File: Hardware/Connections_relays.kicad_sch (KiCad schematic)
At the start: 58 parts, among them J1 USB4105-GF-A-120, J2 Conn_01x02, J3 1040310811, J4 Conn_01x02, J6 Conn_01x02, J7 Conn_01x02, Q2 NMOS, Q3 NMOS, Q4 NMOS, Q5 NMOS, U11 W25Q128JVS, U4 TPD2EUSB30DRTR

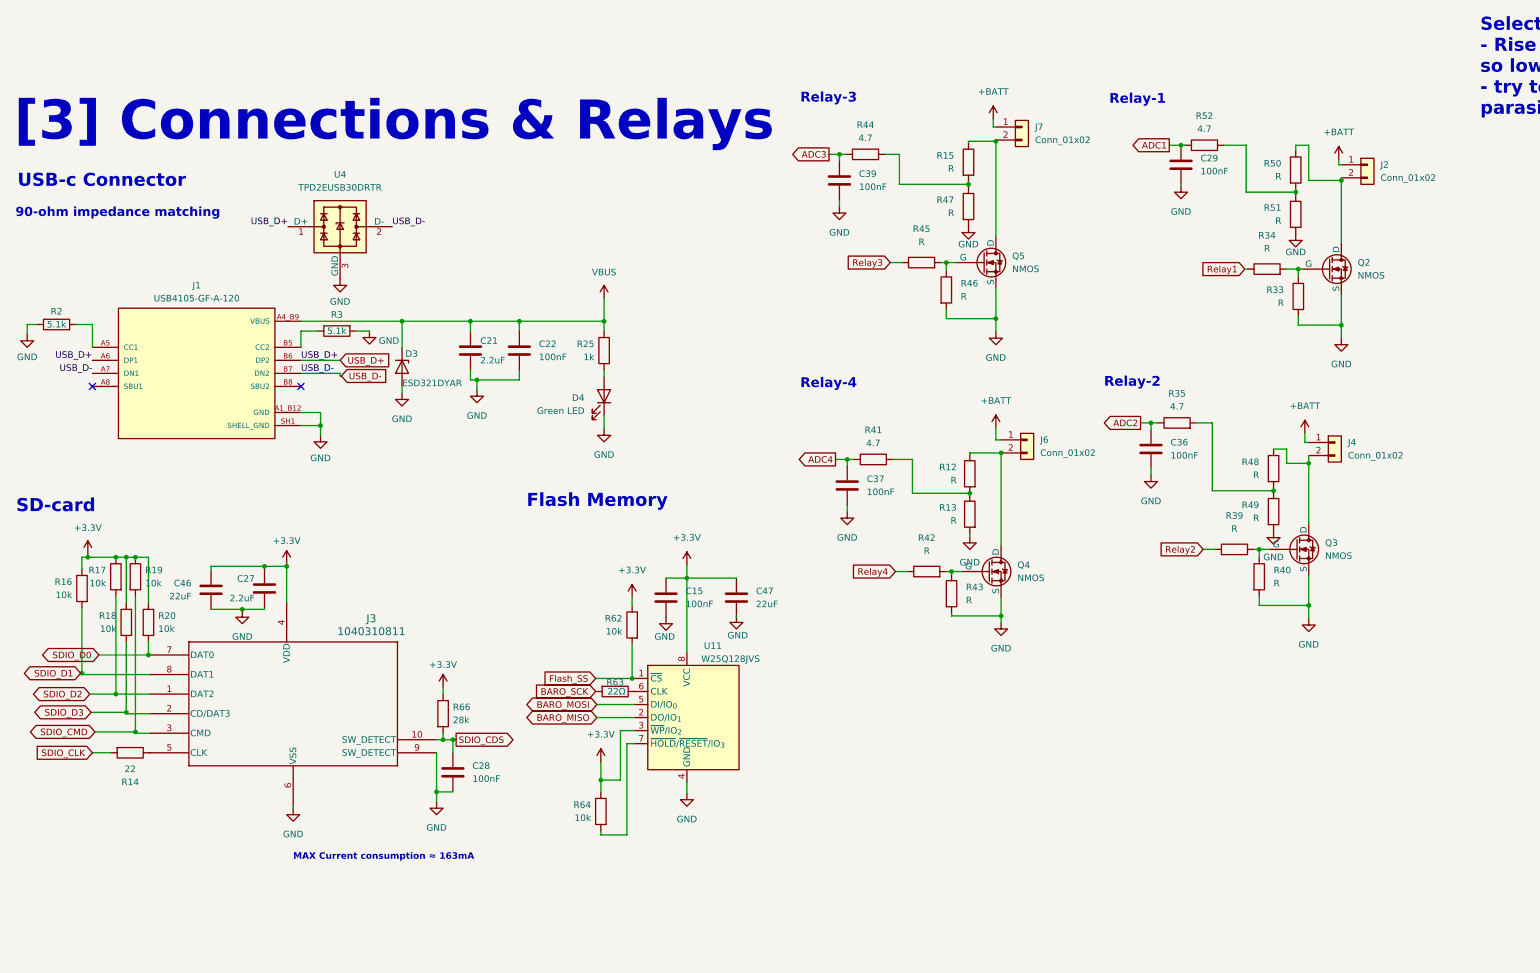
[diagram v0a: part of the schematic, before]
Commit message: Added New file for additional resources used, Changed LDO for lower noise, changed buck converter for higher switching speed, smaller inductance value, better transient current response
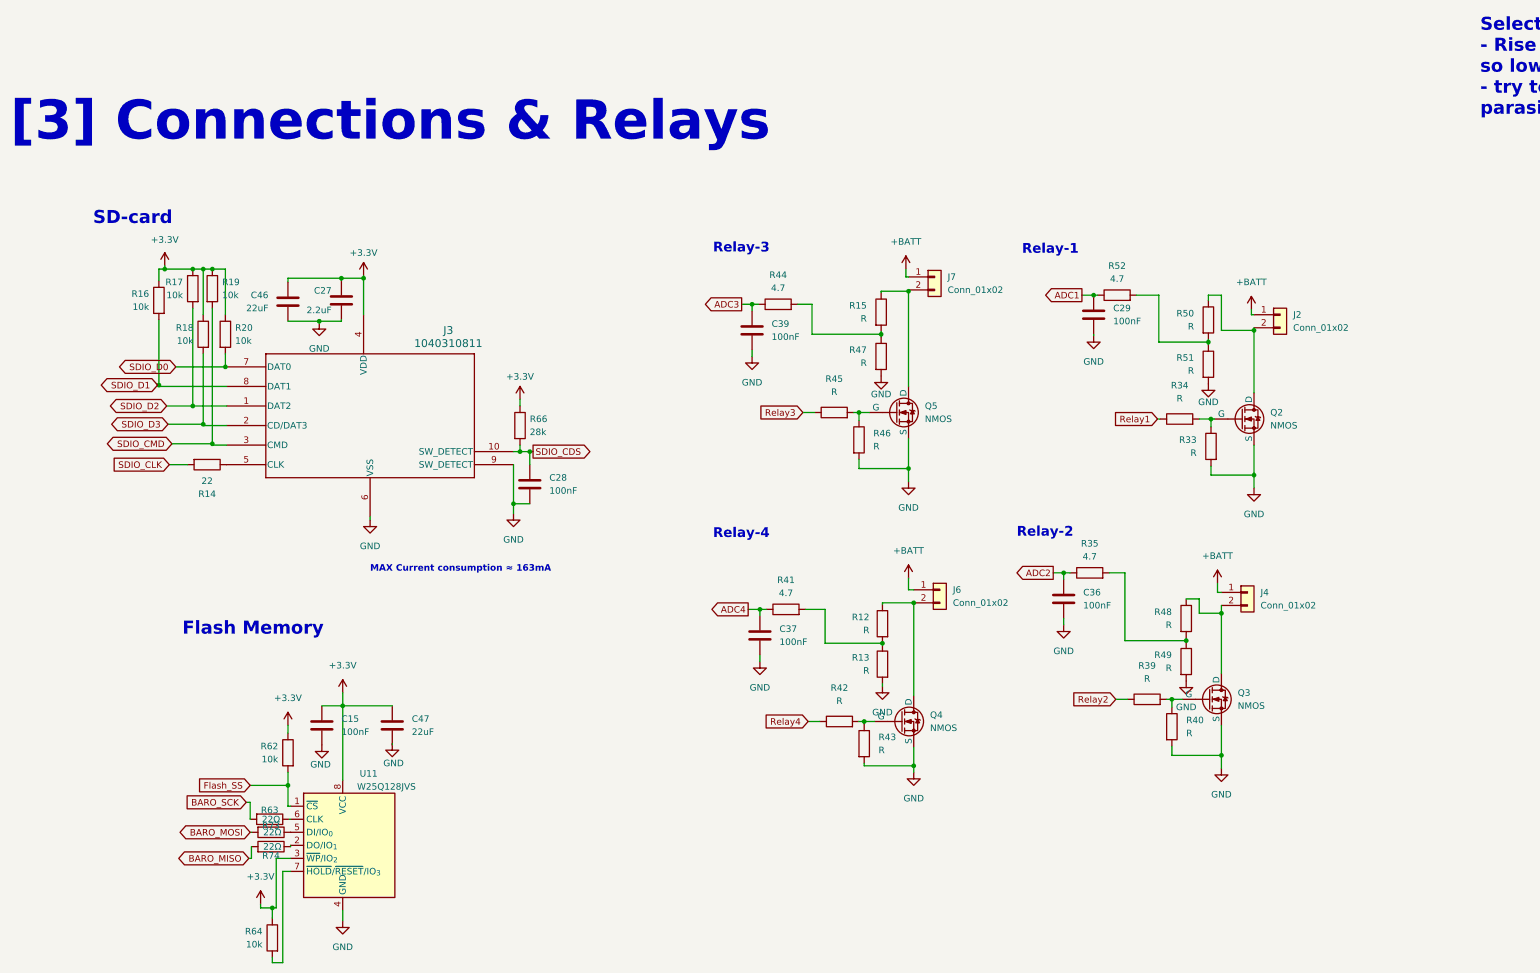
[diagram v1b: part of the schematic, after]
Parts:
- removed C21: 2.2uF, Capacitor_SMD:C_0402_1005Metric, symbol Device:C
- removed C22: 100nF, Capacitor_SMD:C_0402_1005Metric, symbol Device:C
- removed D3: ESD321DYAR, Diode_SMD:D_SOD-523, symbol Diode:ESD5Zxx
- removed D4: Green LED, LED_SMD:LED_0603_1608Metric, symbol Device:LED
- removed J1: USB4105-GF-A-120, USB4105-GF-A-120:GCT_USB4105-GF-A-120, symbol USB4105-GF-A-120:USB4105-GF-A-120
- removed R2, R3: 5.1k, Resistor_SMD:R_0402_1005Metric, symbol Device:R
- removed R25: 1k, Resistor_SMD:R_0402_1005Metric, symbol Device:R
- removed U4: TPD2EUSB30DRTR, Package_TO_SOT_SMD:Texas_DRT-3, symbol Power_Protection:TPD2EUSB30A
- added R73, R74: 22Ω, Resistor_SMD:R_0402_1005Metric, symbol Device:R
- U11: Distributer Link (none) -> https://www.ozdisan.com/en/p/embedded-memories-255/winbond-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; Part Number (none) -> W25Q32RVSSJQ
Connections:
- net BARO_MISO: now also R74.2; no longer U11.2 (DO/IO_{1})
- net BARO_MOSI: now also R73.2; no longer U11.5 (DI/IO_{0})
- new net: R73.1, U11.5 (DI/IO_{0})
- new net: R74.1, U11.2 (DO/IO_{1})
- no-connect marks 2 -> 0
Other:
- note removed: "90-ohm impedance matching"
- note removed: "USB-c Connector"
- moved on the sheet: C15, C27, C28, C29, C36, C37, C39, C46, C47, J2, J3, J4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

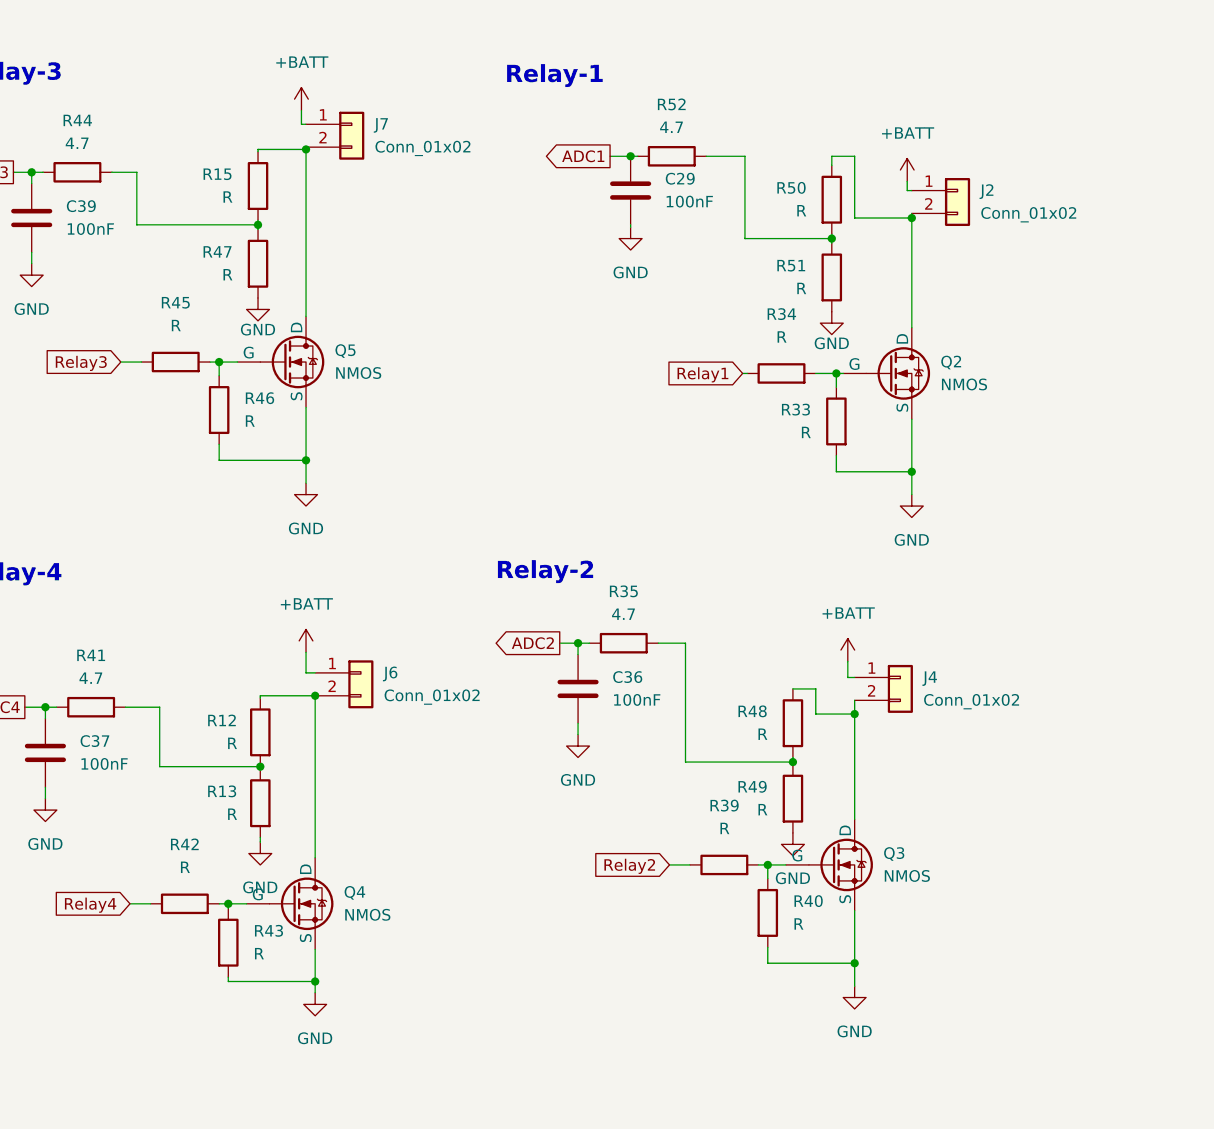
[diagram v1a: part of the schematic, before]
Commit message: Added Impedance matching calculations, finished buck converter calculations, finalized buzzer circuitry
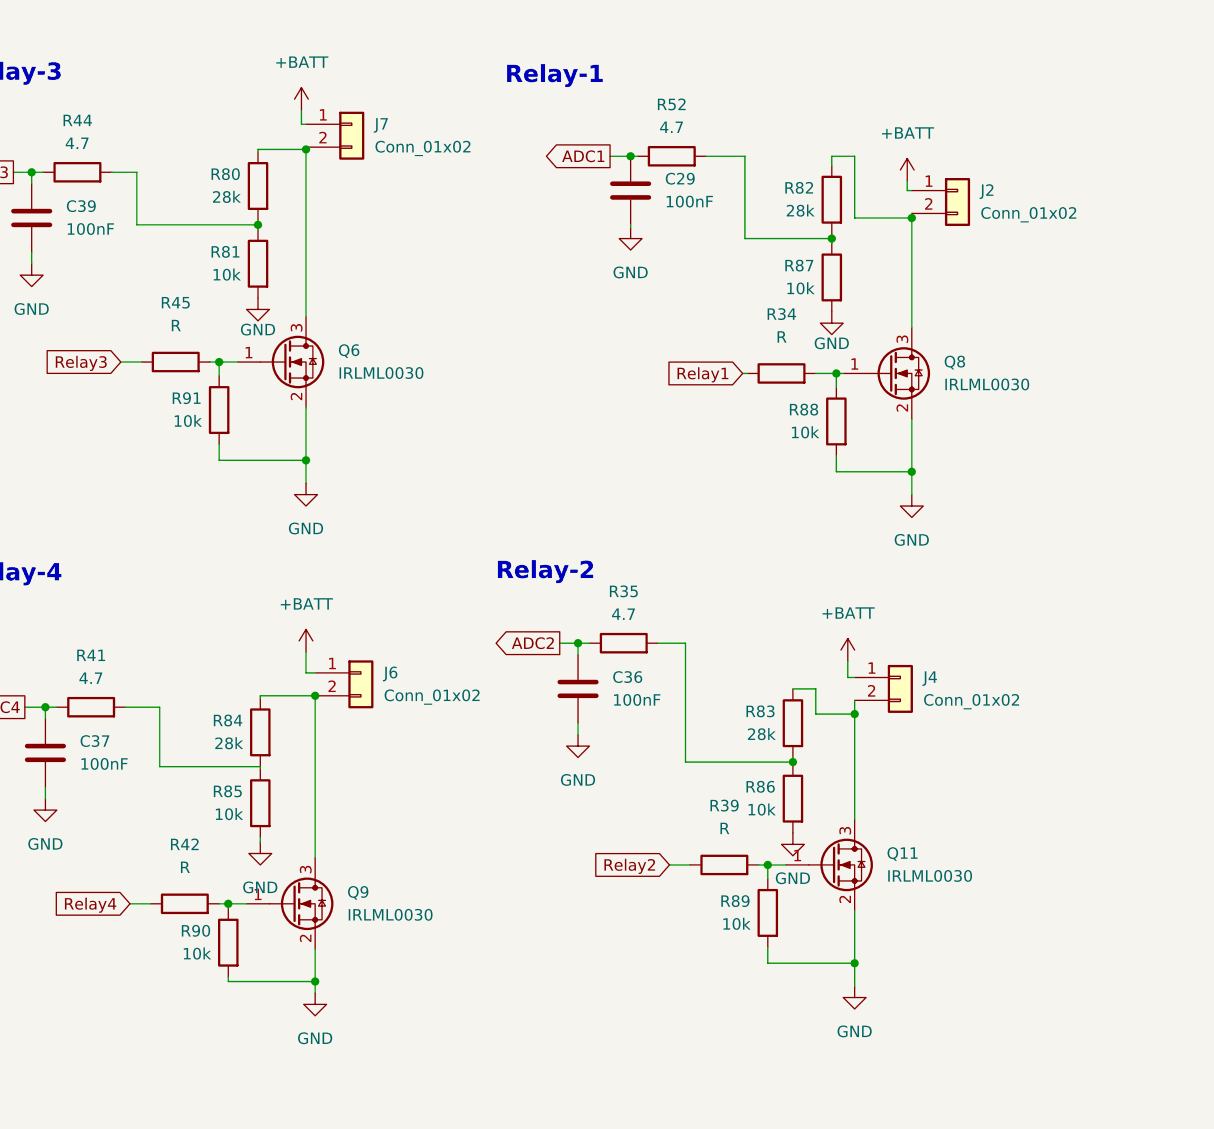
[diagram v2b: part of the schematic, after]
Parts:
- removed Q2, Q3, Q4, Q5: NMOS, symbol Simulation_SPICE:NMOS
- removed R12, R13, R15, R33, R40, R43, R46, R47, R48, R49, R50, R51: R, symbol Device:R
- added Q11, Q6, Q8, Q9: IRLML0030, Package_TO_SOT_SMD:SOT-23, symbol Transistor_FET:IRLML0030
- added R80, R82, R83, R84: 28k, Resistor_SMD:R_0402_1005Metric, symbol Device:R
- added R81, R85, R86, R87, R88, R89, R90, R91: 10k, Resistor_SMD:R_0402_1005Metric, symbol Device:R
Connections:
- net GND: now also Q11.2 (S), Q6.2 (S), Q8.2 (S), Q9.2 (S), R81.2, R85.2, R86.2, R87.2, R88.2, R89.2, R90.2, R91.2
- net at J7.2 (Pin_2): now also Q6.3 (D), R80.1
- net at R45.2: now also Q6.1 (G), R91.1
- net at R42.2: now also Q9.1 (G), R90.1
- net at R39.2: now also Q11.1 (G), R89.1
- net at R35.2: now also R83.2, R86.1
- net at R44.2: now also R80.2, R81.1
- net at R34.2: now also Q8.1 (G), R88.1
- net at R52.2: now also R82.2, R87.1
- net at J6.2 (Pin_2): now also Q9.3 (D), R84.1
- net at R41.2: now also R84.2, R85.1
- net at J4.2 (Pin_2): now also Q11.3 (D), R83.1
- net at J2.2 (Pin_2): now also Q8.3 (D), R82.1

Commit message: Changed footprints, generated BOM
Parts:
- removed R14: 22, Resistor_SMD:R_0402_1005Metric, symbol Device:R
- removed R16, R17, R18, R19, R20, R64: 10k, Resistor_SMD:R_0402_1005Metric, symbol Device:R
- removed R41, R44, R52: 4.7, Resistor_SMD:R_0402_1005Metric, symbol Device:R
- added R105: 22, Resistor_SMD:R_0603_1608Metric, symbol Device:R
- added R36, R37, R38: 4.7, Resistor_SMD:R_0603_1608Metric, symbol Device:R
- added R61, R77, R96, R97, R98, R99: 10k, Resistor_SMD:R_0603_1608Metric, symbol Device:R
- C15, C28, C29, C36, C37, C39: footprint Capacitor_SMD:C_0402_1005Metric -> Capacitor_SMD:C_0603_1608Metric; Distributer Link https://www.ozdisan.com/p/smt-smd-ve-mlcc-kapasitorler-184/murata-grt155r71e104ke01d-1074547 -> https://www.ozdisan.com/p/smt-smd-ve-mlcc-kapasitorler-184/samsung-cl10b104ko8wpnc-522227; Part Number GRT155R71E104KE01D -> CL10B104KO8WPNC
- C27: footprint Capacitor_SMD:C_0402_1005Metric -> Capacitor_SMD:C_0603_1608Metric; Distributer Link http://ozdisan.com/p/smt-smd-ve-mlcc-kapasitorler-184/murat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 -> https://www.ozdisan.com/p/smt-smd-ve-mlcc-kapasitorler-184/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; Part Number GRT155C81A225ME13D -> CL10B225KP8NNNC
- C47: value 22uF -> 2.2uF; footprint Capacitor_SMD:C_0805_2012Metric -> Capacitor_SMD:C_0603_1608Metric; Distributer Link https://www.ozdisan.com/p/smt-smd-ve-mlcc-kapasitorler-184/samsung-cl21a226koqnnne-399002 -> https://www.ozdisan.com/p/smt-smd-ve-mlcc-kapasitorler-184/samsung-cl10b225kp8nnnc-359581; Part Number CL21A226KOQNNNE -> CL10B225KP8NNNC
- J2, J4, J6, J7: now left out of the parts list
- R35: footprint Resistor_SMD:R_0402_1005Metric -> Resistor_SMD:R_0603_1608Metric; Distributer Link https://www.ozdisan.com/p/smt-smd-ve-cip-direncler-194/royalohm-cq02wgj047jtce-587859 -> https://www.ozdisan.com/p/smt-smd-ve-cip-direncler-194/royalohm-cq03saf470kt5e-587940; Part Number CQ02WGJ047JTCE -> CQ03SAF470KT5E
- R62, R88, R89, R90, R91: footprint Resistor_SMD:R_0402_1005Metric -> Resistor_SMD:R_0603_1608Metric; Distributer Link https://www.ozdisan.com/p/smt-smd-ve-cip-direncler-194/roya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 -> https://www.ozdisan.com/p/smt-smd-ve-cip-direncler-194/viki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; Part Number CQ02WGF1002TCE -> CRT03J7E1002
- R81, R85, R86, R87: footprint Resistor_SMD:R_0402_1005Metric -> Resistor_SMD:R_0603_1608Metric; Distributer Link https://www.ozdisan.com/p/smt-smd-ve-cip-direncler-194/royalohm-cq02wgf1002tce-587902 -> https://www.ozdisan.com/p/smt-smd-ve-cip-direncler-194/royalohm-tc0350b1002t5f-700101; Part Number CQ02WGF1002TCE -> TC0350B1002T5F
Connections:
- net +3.3V: now also R61.1, R77.1, R96.1, R97.1, R98.1, R99.1
- net ADC1: now also R37.1
- net ADC3: now also R36.1
- net ADC4: now also R38.1
- net GND: no longer R87.2
- net SDIO_CLK: now also R105.2
- net SDIO_CMD: now also R97.2
- net SDIO_D0: now also R99.2
- net SDIO_D1: now also R77.2
- net SDIO_D2: now also R96.2
- net SDIO_D3: now also R98.2
- net at R80.2, R81.1: now also R36.2
- net at R82.2: now also R37.2; no longer R87.1
- net at J3.5 (CLK): now also R105.1
- net at R84.2, R85.1: now also R38.2
- net at U11.7 (~{HOLD}/~{RESET}/IO_{3}): now also R61.2

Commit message: Final changes
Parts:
- removed R63: 22Ω, Resistor_SMD:R_0402_1005Metric, symbol Device:R
- added R108: 22, Resistor_SMD:R_0603_1608Metric, symbol Device:R
- R73, R74: value 22Ω -> 22; footprint Resistor_SMD:R_0402_1005Metric -> Resistor_SMD:R_0603_1608Metric; Distributer Link https://www.ozdisan.com/p/smt-smd-ve-cip-direncler-194/pana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 -> https://www.ozdisan.com/p/smt-smd-ve-cip-direncler-194/roya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; Part Number ERJ2RKF22R0X -> CQ03SAJ0220T5E
- U11: Distributer Link https://www.ozdisan.com/en/p/embedded-memories-255/winbond-w25q32rvssjq-1580359?https://www.ozdisan.com/?utm_source=google&utm_medium=cpc&utm_campaign=creamake_pmax_en&utm_id=pmax-en&utm_term=%7Bkeyword%7D&utm_content=%7Bcreative%7D&gad_source=1&gad_campaignid=23758541728&gbraid=0AAAAADZaco-i9M5R6brnkfVhGNlfT6Ale&gclid=CjwKCAjw1IHTBhAaEiwA4AYNFgRblH-C799E_ndVsOY2spQbJEYXRXQi4HYBZksWK32CZ7DiI7YqRhoC9D4QAvD_BwE -> https://www.ozdisan.com/en/p/embedded-memories-255/winbond-w25q128jvsiq-525521; Part Number W25Q32RVSSJQ -> W25Q128JVSIQ
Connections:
- net BARO_SCK: now also R108.2
- net at U11.6 (CLK): now also R108.1

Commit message: Final touches
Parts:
- removed R66, R80, R82, R83, R84: 28k, Resistor_SMD:R_0402_1005Metric, symbol Device:R
- added R40, R41, R43, R44, R46: 28k, Resistor_SMD:R_0603_1608Metric, symbol Device:R
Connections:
- net +3.3V: now also R40.1
- net SDIO_CDS: now also R40.2
- net at J7.2 (Pin_2), Q6.3 (D): now also R41.1
- net at R37.2: now also R46.2
- net at R35.2, R86.1: now also R44.2
- net at J6.2 (Pin_2), Q9.3 (D): now also R43.1
- net at R38.2, R85.1: now also R43.2
- net at J4.2 (Pin_2), Q11.3 (D): now also R44.1
- net at R36.2, R81.1: now also R41.2
- net at J2.2 (Pin_2), Q8.3 (D): now also R46.1

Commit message: Purged heavy binaries and updated gitignore
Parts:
- removed C46: 22uF, Capacitor_SMD:C_0805_2012Metric, symbol Device:C
- removed J2, J4, J6: Conn_01x02, symbol Connector_Generic:Conn_01x02
- removed J3: 1040310811, Molex 1040310811:104031-0811_MOL, symbol 2026-07-10_16-12-29:1040310811
- removed R108, R73: 22, Resistor_SMD:R_0603_1608Metric, symbol Device:R
- removed R34, R39, R42: R, symbol Device:R
- added C62: 22uF, Capacitor_SMD:C_0805_2012Metric, symbol Device:C
- added J10, J11, J9: Conn_01x02, ICM_42688_P:E-match_Solder, symbol Connector_Generic:Conn_01x02
- added J4: 1040310811, Molex 1040310811:104031-0811_MOL, symbol 2026-07-10_16-12-29:1040310811
- added R109, R110, R111, R112, R113, R117: 22, Resistor_SMD:R_0603_1608Metric, symbol Device:R
- added R47, R48, R49: 300, Resistor_SMD:R_0603_1608Metric, symbol Device:R
- J7: footprint (none) -> ICM_42688_P:E-match_Solder
- R45: value R -> 300; footprint (none) -> Resistor_SMD:R_0603_1608Metric; Distributer Link (none) -> https://www.ozdisan.com/p/smt-smd-ve-cip-direncler-194/pana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; Part Number (none) -> ERJ3EKF3000V
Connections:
- net +3.3V: now also C62.1, J4.4 (VDD)
- net +BATT: now also J10.1 (Pin_1), J11.1 (Pin_1), J9.1 (Pin_1)
- net Flash_SS: now also R117.2; no longer R62.2, U11.1 (~{CS})
- net GND: now also R87.2, C62.2, J4.11 (MP), J4.12 (MP), J4.13 (MP), J4.14 (MP), J4.6 (GND), J4.9 (SW_DETECT)
- net Relay1: now also R47.1
- net Relay2: now also R48.1
- net Relay4: now also R49.1
- net SDIO_CDS: now also J4.10 (SW_DETECT)
- net SDIO_CMD: now also R109.2; no longer R97.2
- net SDIO_D0: now also R113.2; no longer R99.2
- net SDIO_D1: now also R112.2; no longer R77.2
- net SDIO_D2: now also R111.2; no longer R96.2
- net SDIO_D3: now also R110.2; no longer R98.2
- net at Q9.3 (D), R43.1: now also J11.2 (Pin_2)
- net at Q11.3 (D), R44.1: now also J10.2 (Pin_2)
- net at Q11.1 (G), R89.1: now also R48.2
- net at Q8.1 (G), R88.1: now also R47.2
- net at R37.2, R46.2: now also R87.1
- net Acc_flash_MOSI: now reaches U11.5 (DI/IO_{0})
- net at Q9.1 (G), R90.1: now also R49.2
- net at R105.1: now also J4.5 (CLK)
- net at Q8.3 (D), R46.1: now also J9.2 (Pin_2)
- net Acc_flash_CLK: now reaches U11.6 (CLK)
- net BARO_MISO renamed Acc_flash_MISO
- new net: J4.7 (DAT0), R113.1, R99.2
- new net: J4.2 (CD/DAT3), R110.1, R96.2
- new net: J4.1 (DAT2), R111.1, R98.2
- new net: R117.1, R62.2, U11.1 (~{CS})
- new net: J4.3 (CMD), R109.1, R77.2
- new net: J4.8 (DAT1), R112.1, R97.2
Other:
- note removed: "Select gate resistors so that: - Rise and fall time are small so low power dissipation on mosfet - try to achieve critically damped oscillation caused by parasitic inductance and capacitance"
- moved on the sheet: C15, C27, C28, C29, C36, C37, C39, C47, J7, Q11, Q6, Q8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
